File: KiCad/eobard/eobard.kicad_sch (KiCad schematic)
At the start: 20 parts, among them J1 UART JACK LEFT, J3 UART Jack Right, SW1 SW_SPST, SW10 SW_SPST, SW11 SW_SPST, SW12 SW_SPST, SW13 SW_SPST, SW14 SW_SPST, SW15 SW_SPST, SW16 SW_SPST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

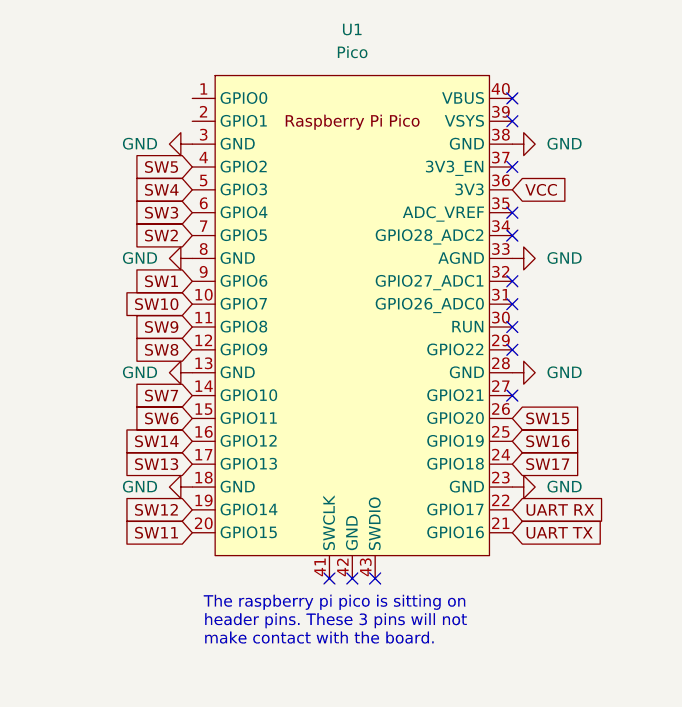
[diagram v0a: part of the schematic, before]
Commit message: Finished Initial Board Layout
Improving on the prototype. Gerbers are inside kicad folder.
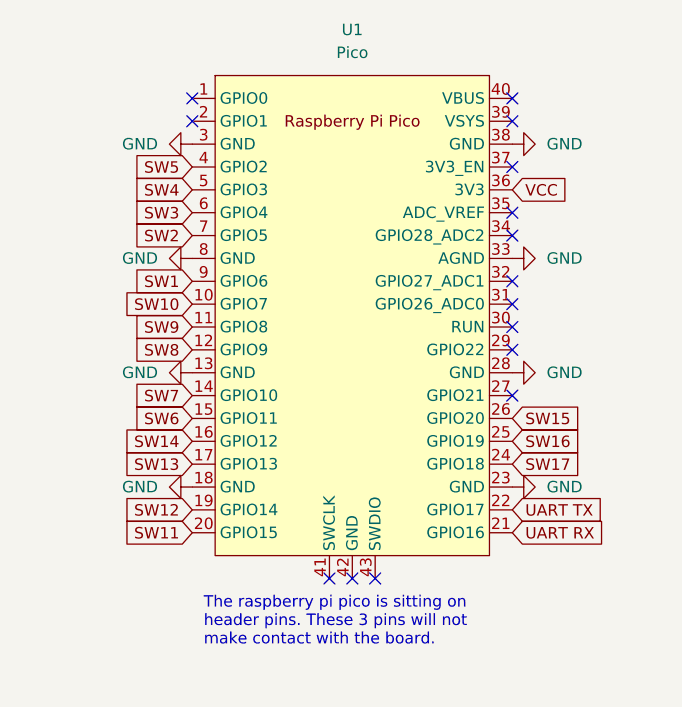
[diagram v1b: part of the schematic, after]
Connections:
- net UART RX: now also U1.21 (GPIO16); no longer U1.22 (GPIO17)
- net UART TX: now also U1.22 (GPIO17); no longer U1.21 (GPIO16)
- no-connect marks 13 -> 15
